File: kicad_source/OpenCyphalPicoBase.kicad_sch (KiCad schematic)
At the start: 50 parts, among them CN1 RASPBERRYPI_PICO, CN2 SM04B-SRSS-TB, CN3 SM04B-SRSS-TB, CN6 691322310002, CN7 CONN_02X03, CN8 01X08, CN9 1x04, SW1 SPST, U3 24LC64

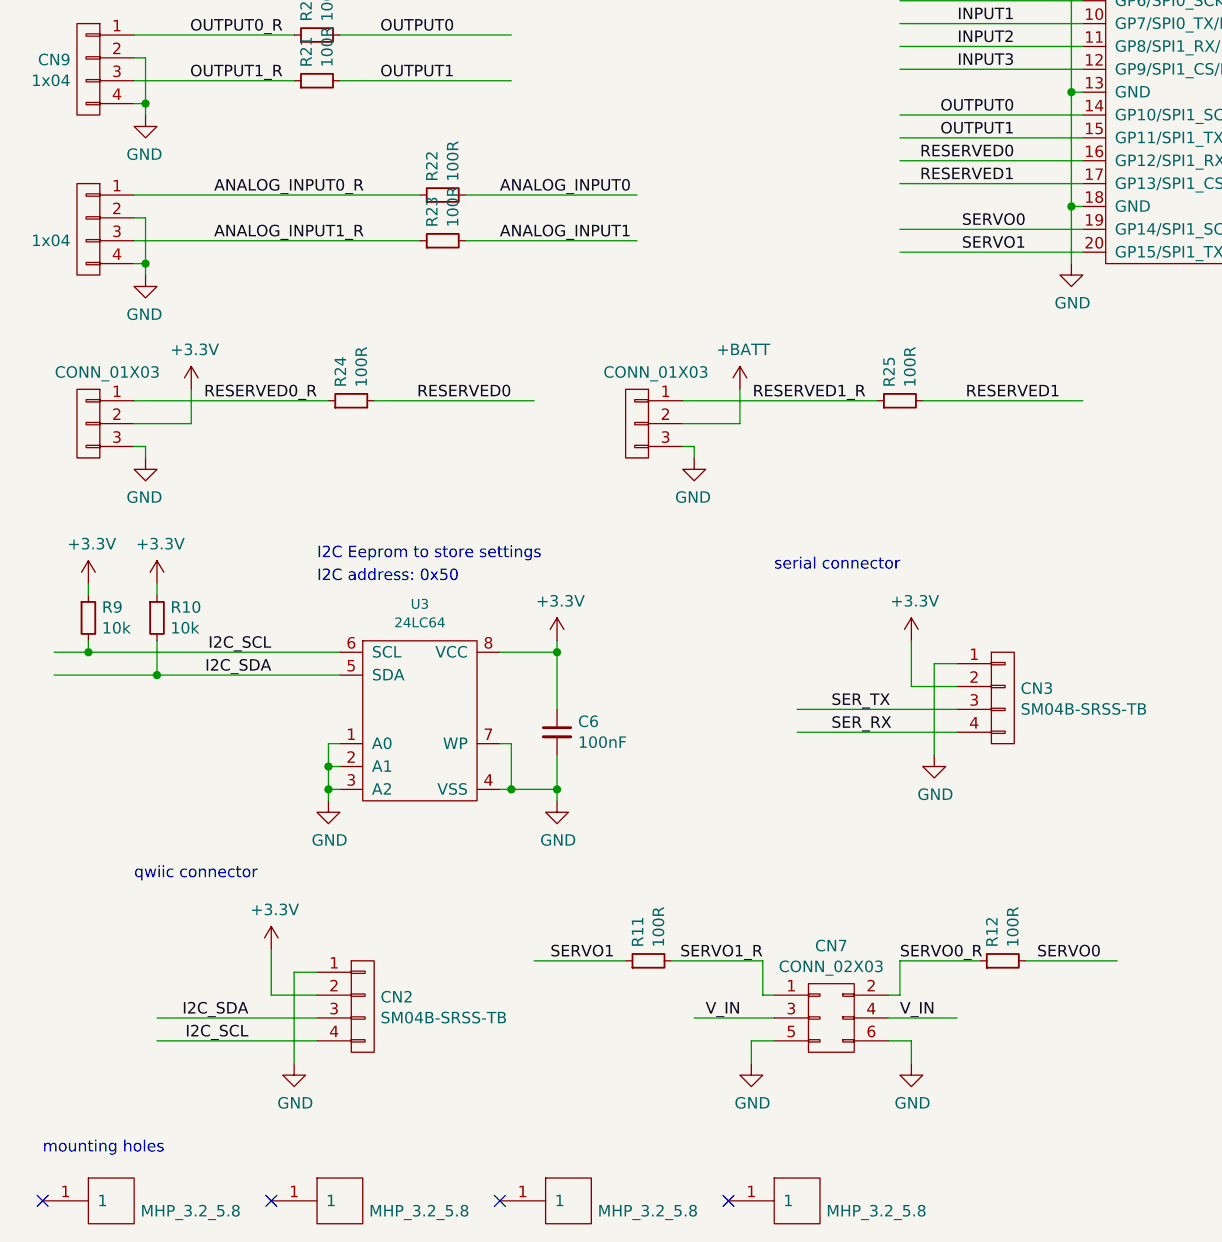
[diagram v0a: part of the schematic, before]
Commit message: removed some tht parts
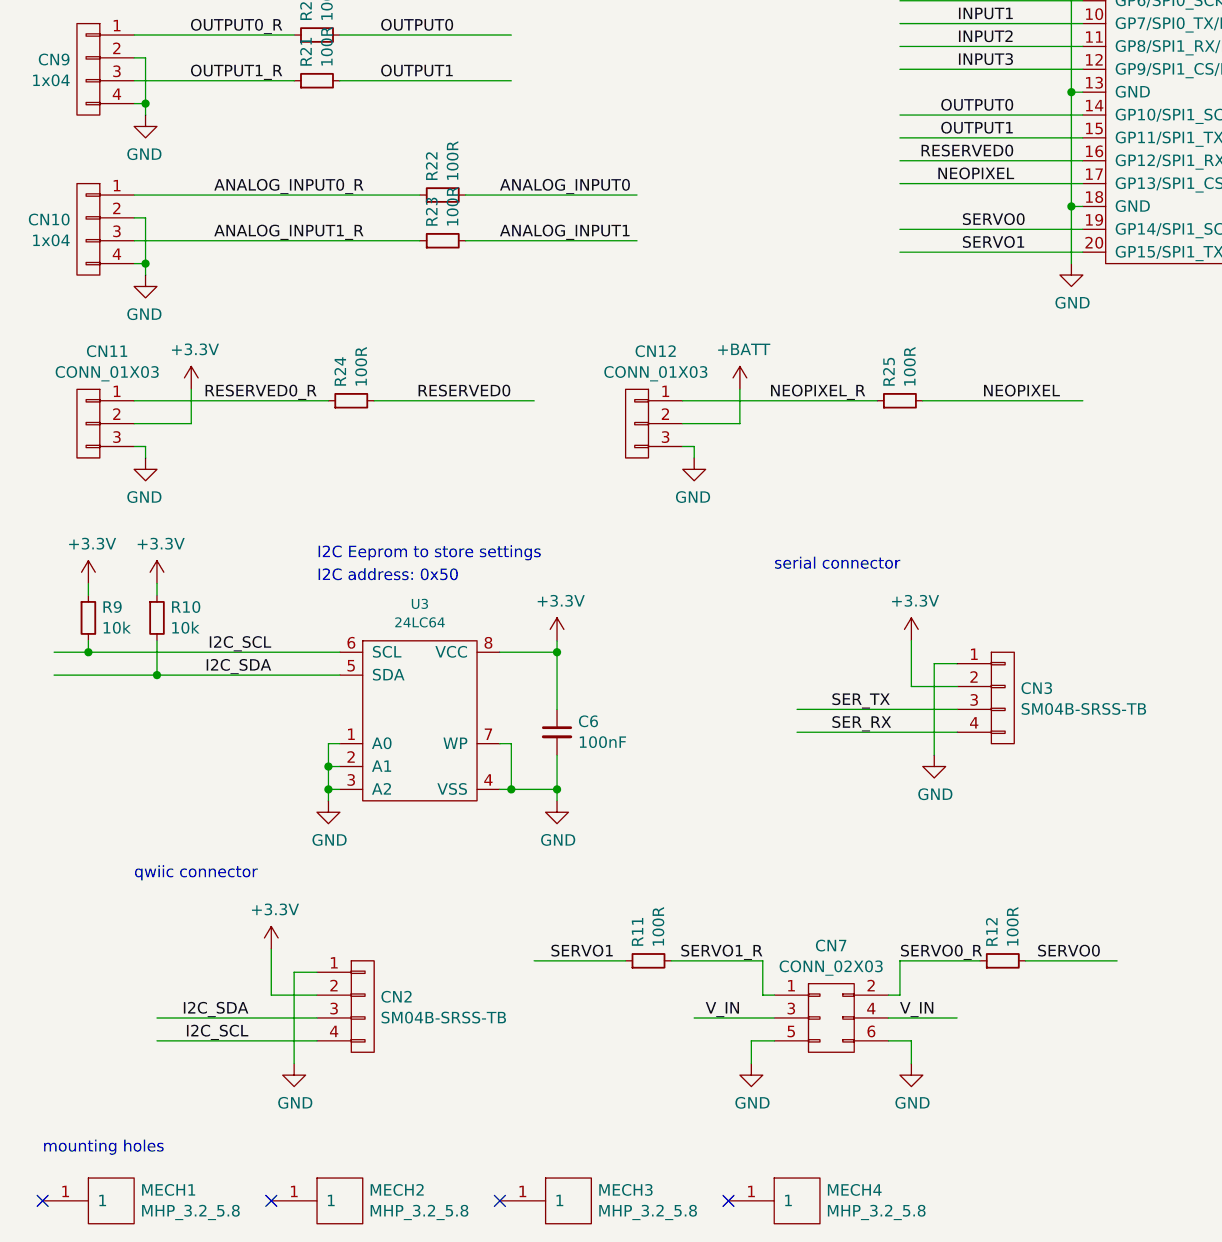
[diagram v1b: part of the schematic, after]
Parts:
- gave numbers to parts that had none: 7
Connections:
- net RESERVED1 renamed NEOPIXEL
- net RESERVED1_R renamed NEOPIXEL_R
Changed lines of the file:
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@@
   (title_block
     (title "OpenCyphalPicoBase")
-    (date "2022-06-10")
-    (rev "0.1")
+    (date "2022-10-09")
+    (rev "0.2")
     (company "generationmake")
   )
@@
     (effects (font (size 1.27 1.27)) (justify left bottom))
   )
-  (label "RESERVED1_R" (at 109.22 104.14 180)
+  (label "NEOPIXEL_R" (at 109.22 104.14 180)
     (effects (font (size 1.27 1.27)) (justify right bottom))
   )
@@
     (effects (font (size 1.27 1.27)) (justify left bottom))
   )
-  (label "RESERVED1" (at 130.81 104.14 180)
+  (label "NEOPIXEL" (at 130.81 104.14 180)
     (effects (font (size 1.27 1.27)) (justify right bottom))
   )
@@
     (effects (font (size 1.27 1.27)) (justify left bottom))
   )
-  (label "RESERVED1" (at 125.73 80.01 180)
+  (label "NEOPIXEL" (at 125.73 80.01 180)
     (effects (font (size 1.27 1.27)) (justify right bottom))
   )
@@
   (symbol (lib_id "OpenCyphalPicoBase-rescue:MHP_3.2_5.8-MECH_mounting-holes") (at 25.4 193.04 0) (unit 1)
     (in_bom yes) (on_board yes)
-    (property "Reference" "" (id 0) (at 28.6512 191.8716 0)
+    (property "Reference" "MECH1" (id 0) (at 28.6512 191.8716 0)
       (effects (font (size 1.27 1.27)) (justify left))
     )
@@
   (symbol (lib_id "OpenCyphalPicoBase-rescue:MHP_3.2_5.8-MECH_mounting-holes") (at 50.8 193.04 0) (unit 1)
     (in_bom yes) (on_board yes)
-    (property "Reference" "" (id 0) (at 54.0512 191.8716 0)
+    (property "Reference" "MECH2" (id 0) (at 54.0512 191.8716 0)
       (effects (font (size 1.27 1.27)) (justify left))
     )
@@
   (symbol (lib_id "OpenCyphalPicoBase-rescue:MHP_3.2_5.8-MECH_mounting-holes") (at 76.2 193.04 0) (unit 1)
     (in_bom yes) (on_board yes)
-    (property "Reference" "" (id 0) (at 79.4512 191.8716 0)
+    (property "Reference" "MECH3" (id 0) (at 79.4512 191.8716 0)
       (effects (font (size 1.27 1.27)) (justify left))
     )
@@
   (symbol (lib_id "OpenCyphalPicoBase-rescue:MHP_3.2_5.8-MECH_mounting-holes") (at 101.6 193.04 0) (unit 1)
     (in_bom yes) (on_board yes)
-    (property "Reference" "" (id 0) (at 104.8512 191.8716 0)
+    (property "Reference" "MECH4" (id 0) (at 104.8512 191.8716 0)
       (effects (font (size 1.27 1.27)) (justify left))
     )
@@
   (symbol (lib_id "OpenCyphalPicoBase-rescue:+3.3V-power-supply") (at 114.3 130.81 0) (unit 1)
     (in_bom yes) (on_board yes)
-    (property "Reference" "" (id 0) (at 114.3 134.62 0)
+    (property "Reference" "#PWR039" (id 0) (at 114.3 134.62 0)
       (effects (font (size 1.27 1.27)) hide)
     )
@@
   (symbol (lib_id "OpenCyphalPicoBase-rescue:+3.3V-power-supply") (at 22.86 124.46 0) (unit 1)
     (in_bom yes) (on_board yes)
-    (property "Reference" "" (id 0) (at 22.86 128.27 0)
+    (property "Reference" "#PWR041" (id 0) (at 22.86 128.27 0)
       (effects (font (size 1.27 1.27)) hide)
     )
@@
   (symbol (lib_id "OpenCyphalPicoBase-rescue:+3.3V-power-supply") (at 30.48 124.46 0) (unit 1)
     (in_bom yes) (on_board yes)
-    (property "Reference" "" (id 0) (at 30.48 128.27 0)
+    (property "Reference" "#PWR042" (id 0) (at 30.48 128.27 0)
       (effects (font (size 1.27 1.27)) hide)
     )
@@
   (symbol (lib_id "OpenCyphalPicoBase-rescue:+3.3V-power-supply") (at 43.18 165.1 0) (unit 1)
     (in_bom yes) (on_board yes)
-    (property "Reference" "" (id 0) (at 43.18 168.91 0)
+    (property "Reference" "#PWR019" (id 0) (at 43.18 168.91 0)
       (effects (font (size 1.27 1.27)) hide)
     )
@@
   (symbol (lib_id "OpenCyphalPicoBase-rescue:+3.3V-power-supply") (at 74.93 130.81 0) (unit 1)
     (in_bom yes) (on_board yes)
-    (property "Reference" "" (id 0) (at 74.93 134.62 0)
+    (property "Reference" "#PWR016" (id 0) (at 74.93 134.62 0)
       (effects (font (size 1.27 1.27)) hide)
     )
@@
   (symbol (lib_id "OpenCyphalPicoBase-rescue:+BATT-power-supply") (at 165.1 133.35 0) (unit 1)
     (in_bom yes) (on_board yes)
-    (property "Reference" "" (id 0) (at 165.1 137.16 0)
+    (property "Reference" "#PWR020" (id 0) (at 165.1 137.16 0)
       (effects (font (size 1.27 1.27)) hide)
     )
@@
   (symbol (lib_id "OpenCyphalPicoBase-rescue:+BATT-power-supply") (at 217.17 41.91 270) (unit 1)
     (in_bom yes) (on_board yes)
-    (property "Reference" "" (id 0) (at 213.36 41.91 0)
+    (property "Reference" "#PWR015" (id 0) (at 213.36 41.91 0)
       (effects (font (size 1.27 1.27)) hide)
     )
@@
   (symbol (lib_id "OpenCyphalPicoBase-rescue:+BATT-power-supply") (at 260.35 41.91 0) (unit 1)
     (in_bom yes) (on_board yes)
-    (property "Reference" "" (id 0) (at 260.35 45.72 0)
+    (property "Reference" "#PWR043" (id 0) (at 260.35 45.72 0)
       (effects (font (size 1.27 1.27)) hide)
     )
@@
   (symbol (lib_id "OpenCyphalPicoBase-rescue:+3.3V-power-supply") (at 35.56 19.05 0) (mirror y) (unit 1)
     (in_bom yes) (on_board yes)
-    (property "Reference" "" (id 0) (at 35.56 22.86 0)
+    (property "Reference" "#PWR03" (id 0) (at 35.56 22.86 0)
       (effects (font (size 1.27 1.27)) hide)
     )
@@
   (symbol (lib_id "OpenCyphalPicoBase-rescue:+3.3V-power-supply") (at 43.18 19.05 0) (mirror y) (unit 1)
     (in_bom yes) (on_board yes)
-    (property "Reference" "" (id 0) (at 43.18 22.86 0)
+    (property "Reference" "#PWR04" (id 0) (at 43.18 22.86 0)
       (effects (font (size 1.27 1.27)) hide)
     )
@@
   (symbol (lib_id "OpenCyphalPicoBase-rescue:+3.3V-power-supply") (at 50.8 19.05 0) (mirror y) (unit 1)
     (in_bom yes) (on_board yes)
-    (property "Reference" "" (id 0) (at 50.8 22.86 0)
+    (property "Reference" "#PWR06" (id 0) (at 50.8 22.86 0)
       (effects (font (size 1.27 1.27)) hide)
     )
@@
   (symbol (lib_id "OpenCyphalPicoBase-rescue:+3.3V-power-supply") (at 58.42 19.05 0) (mirror y) (unit 1)
     (in_bom yes) (on_board yes)
-    (property "Reference" "" (id 0) (at 58.42 22.86 0)
+    (property "Reference" "#PWR07" (id 0) (at 58.42 22.86 0)
       (effects (font (size 1.27 1.27)) hide)
     )
@@
   (symbol (lib_id "OpenCyphalPicoBase-rescue:CONN_01X04-mechanical-connectors") (at 22.86 85.09 0) (mirror y) (unit 1)
     (in_bom yes) (on_board yes)
-    (property "Reference" "" (id 0) (at 20.8788 84.0486 0)
+    (property "Reference" "CN10" (id 0) (at 20.8788 84.0486 0)
       (effects (font (size 1.27 1.27)) (justify left))
     )
@@
   (symbol (lib_id "OpenCyphalPicoBase-rescue:CONN_01X03-mechanical-connectors") (at 22.86 106.68 0) (mirror y) (unit 1)
     (in_bom yes) (on_board yes)
-    (property "Reference" "" (id 0) (at 24.9682 98.679 0))
+    (property "Reference" "CN11" (id 0) (at 24.9682 98.679 0))
     (property "Value" "CONN_01X03" (id 1) (at 24.9682 100.9904 0))
     (property "Footprint" "pin_headers:Pin_Header_Straight_1x03" (id 2) (at 22.86 106.68 0)
@@
   (symbol (lib_id "OpenCyphalPicoBase-rescue:+3.3V-power-supply") (at 34.29 102.87 0) (unit 1)
     (in_bom yes) (on_board yes)
-    (property "Reference" "" (id 0) (at 34.29 106.68 0)
+    (property "Reference" "#PWR048" (id 0) (at 34.29 106.68 0)
       (effects (font (size 1.27 1.27)) hide)
     )
@@
   (symbol (lib_id "OpenCyphalPicoBase-rescue:CONN_01X03-mechanical-connectors") (at 83.82 106.68 0) (mirror y) (unit 1)
     (in_bom yes) (on_board yes)
-    (property "Reference" "" (id 0) (at 85.9282 98.679 0))
+    (property "Reference" "CN12" (id 0) (at 85.9282 98.679 0))
     (property "Value" "CONN_01X03" (id 1) (at 85.9282 100.9904 0))
     (property "Footprint" "pin_headers:Pin_Header_Straight_1x03" (id 2) (at 83.82 106.68 0)
@@
   (symbol (lib_id "OpenCyphalPicoBase-rescue:+BATT-power-supply") (at 95.25 102.87 0) (unit 1)
     (in_bom yes) (on_board yes)
-    (property "Reference" "" (id 0) (at 95.25 106.68 0)
-      (effects (font (size 1.27 1.27)) hide)
-    )
+    (property "Reference" "#PWR049" (id 0) (at 95.25 106.68 0)
+      (effects (font (size 1.27 1.27)) hide)
+    )

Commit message: switched Raspberry Pi Pico to direct solder only
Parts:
- CN1: footprint MODULE_compute:RASPI_PICO_SOLDER -> generationmake:RASPI_PICO_SOLDER_Kopie
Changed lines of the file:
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@@
     (property "Reference" "CN1" (id 0) (at 172.72 33.655 0))
     (property "Value" "RASPBERRYPI_PICO" (id 1) (at 172.72 35.9664 0))
-    (property "Footprint" "MODULE_compute:RASPI_PICO_SOLDER" (id 2) (at 172.72 63.5 0)
+    (property "Footprint" "generationmake:RASPI_PICO_SOLDER_Kopie" (id 2) (at 172.72 63.5 0)
       (effects (font (size 1.27 1.27)) hide)
     )
@@
     )
     (path "/00000000-0000-0000-0000-0000629e332f"
-      (reference "CN1") (unit 1) (value "RASPBERRYPI_PICO") (footprint "MODULE_compute:RASPI_PICO_SOLDER")
+      (reference "CN1") (unit 1) (value "RASPBERRYPI_PICO") (footprint "generationmake:RASPI_PICO_SOLDER_Kopie")
     )
     (path "/00000000-0000-0000-0000-00006250ded9"

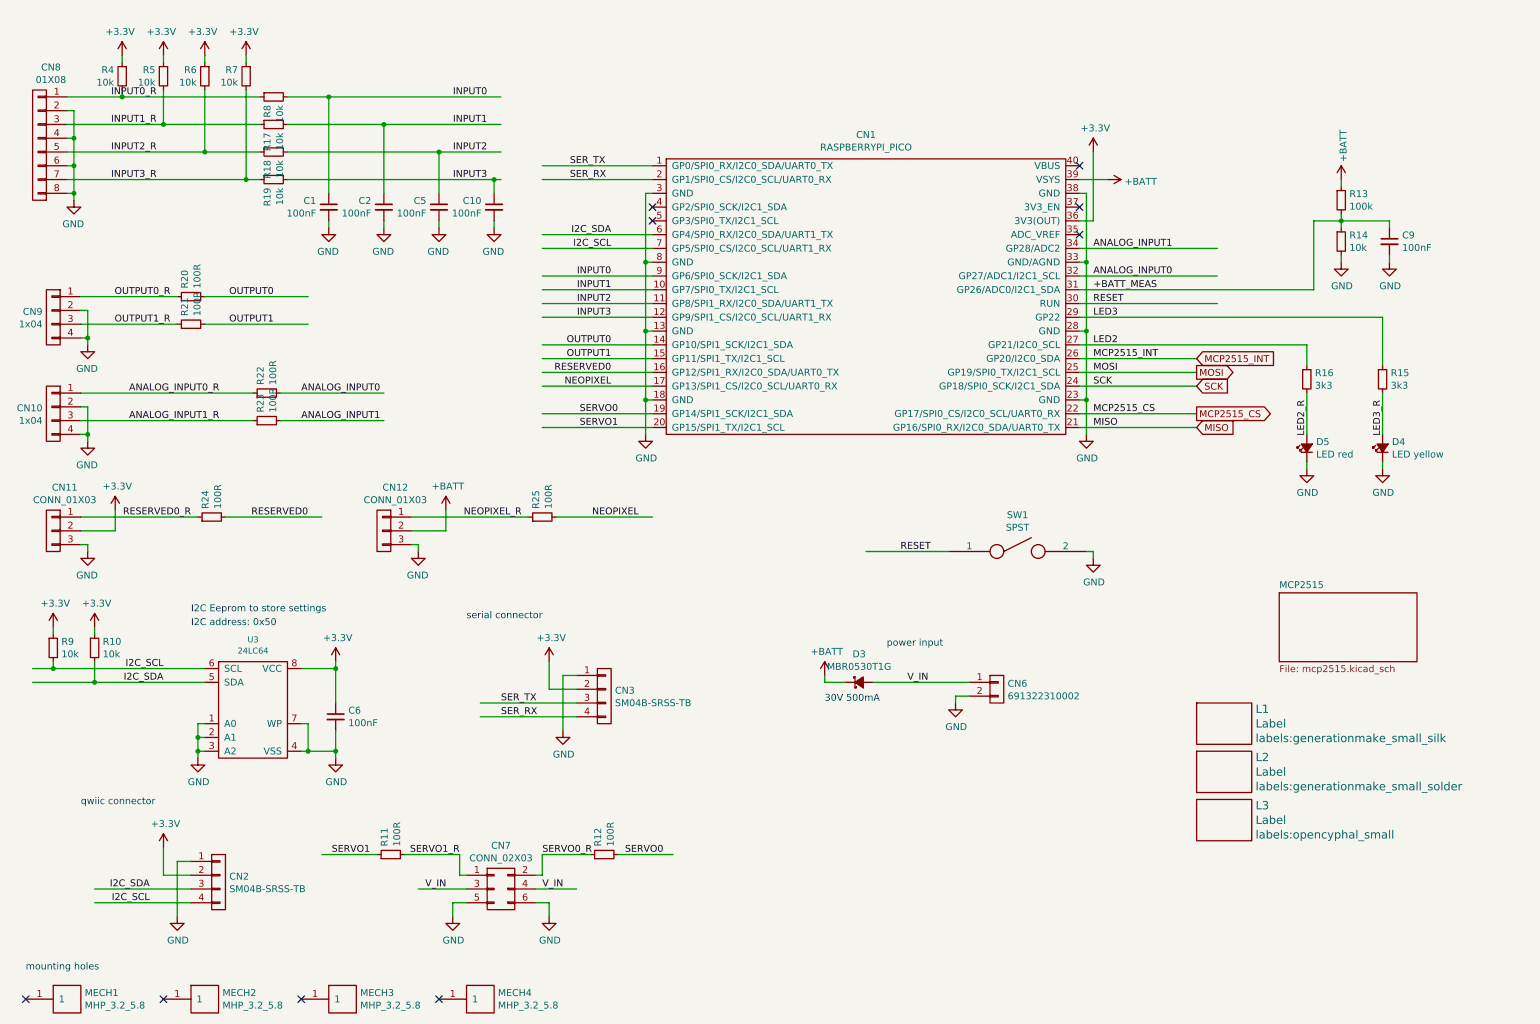
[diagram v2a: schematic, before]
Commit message: reworked library references
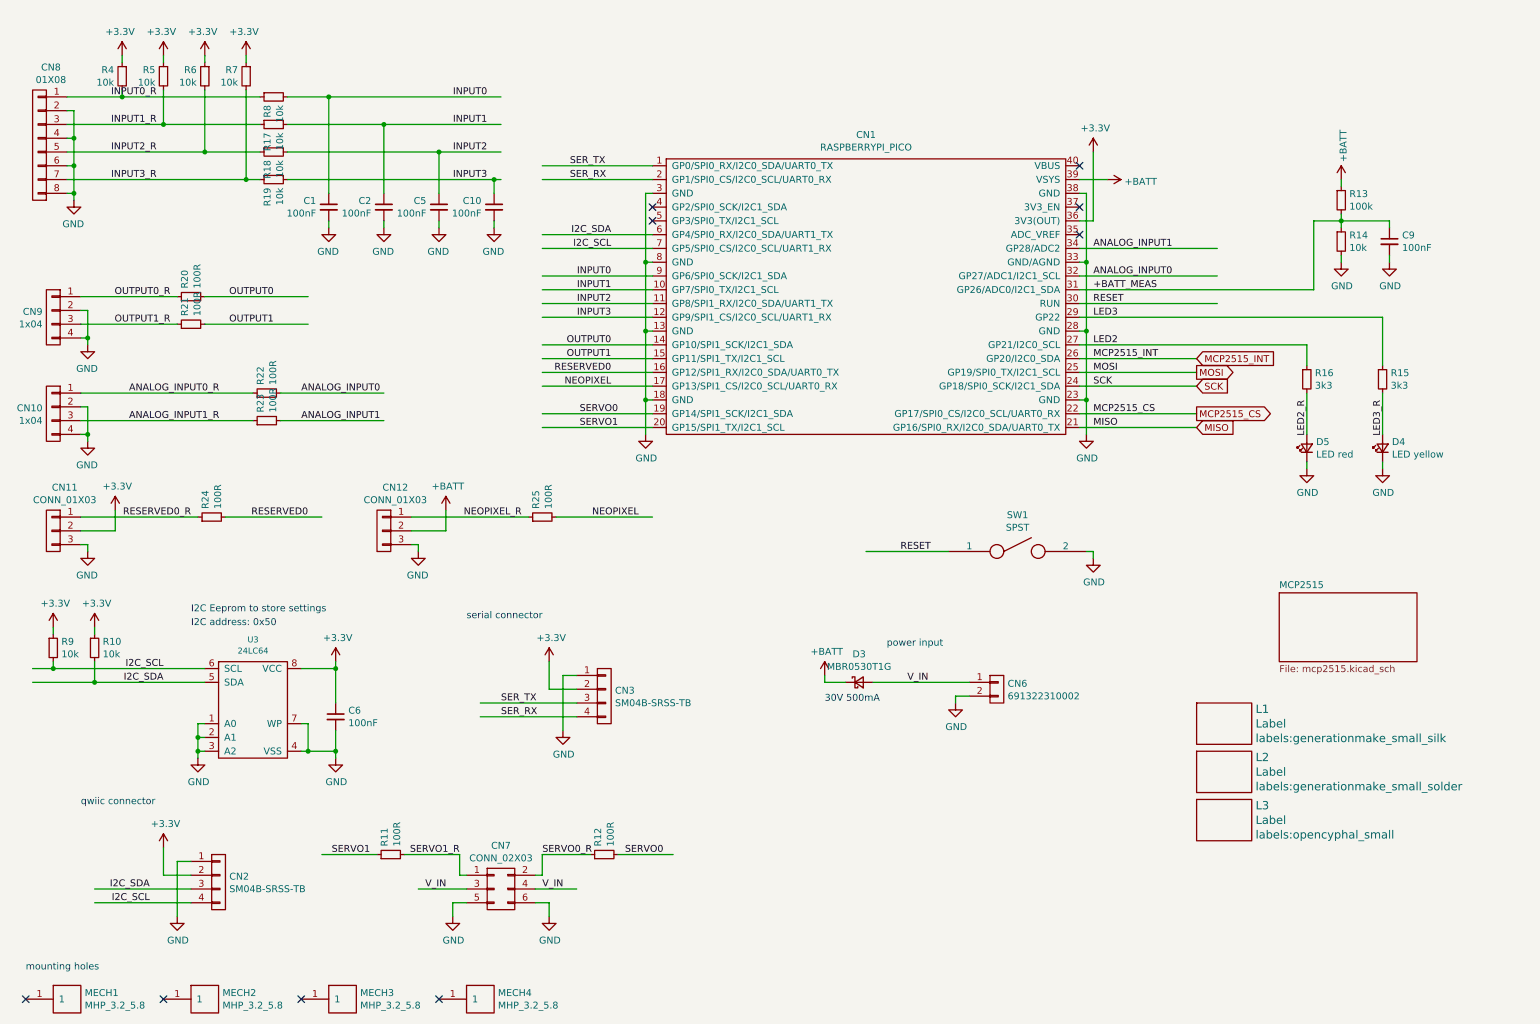
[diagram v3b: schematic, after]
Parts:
- C1, C10, C2, C5, C6, C9: footprint capacitors:C_0603 -> Capacitor_SMD:C_0603_1608Metric; symbol OpenCyphalPicoBase-rescue:C_0603-devices -> Device:C_Small
- CN2, CN3: footprint connectors_JST_SH:Connectors_JST_SM04B-SRSS-TB -> Connector_JST:JST_SH_SM04B-SRSS-TB_1x04-1MP_P1.00mm_Horizontal
- D3: footprint diodes:SOD-123 -> Diode_SMD:D_SOD-123; symbol OpenCyphalPicoBase-rescue:D_Schottky_Small-devices -> Device:D_Schottky_Small
- D4, D5: footprint LEDs:LED_0603 -> LED_SMD:LED_0603_1608Metric; symbol OpenCyphalPicoBase-rescue:Led_Small-devices -> Device:LED_Small
- R10, R11, R12, R13, R14, R15, R16, R17, R18, R19, R20, R21, R22, R23, R24, R25, R4, R5, R6, R7, R8, R9: footprint resistors:R_0603 -> Resistor_SMD:R_0603_1608Metric; symbol OpenCyphalPicoBase-rescue:R_0603-devices -> Device:R_Small
- U3: footprint SOIC:SOIC-8_3.9x4.9mm_Pitch1.27mm -> Package_SO:SOIC-8_3.9x4.9mm_P1.27mm
